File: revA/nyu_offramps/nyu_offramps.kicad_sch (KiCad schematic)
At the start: 88 parts, among them J15 Conn_02x06_Odd_Even, J16 Conn_01x24_Female, J17 Conn_01x24_Female, J19 Conn_01x06_Male, J23 Screw_Terminal_01x02, J24 Conn_01x03_Male, J25 Screw_Terminal_01x02, J3 Conn_01x04_Pin, J4 Conn_01x01, U1 MCP4725xxx-xCH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

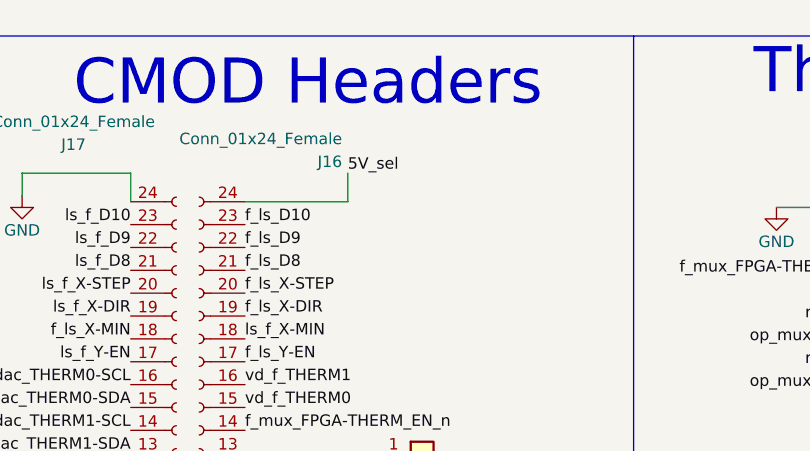
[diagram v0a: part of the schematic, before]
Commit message: Cleaned up and renamed project
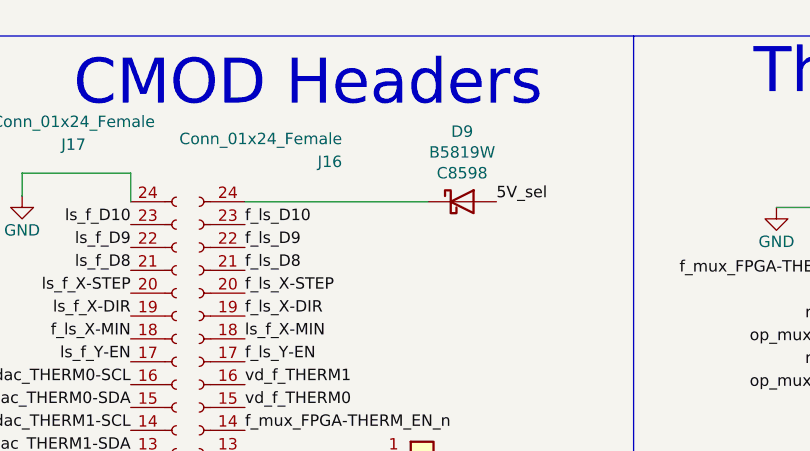
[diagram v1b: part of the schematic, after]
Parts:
- added D9: B5819W, Diode_SMD:D_SOD-123, symbol Device:D_Schottky
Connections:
- net 5V_sel: now also D9.2 (A); no longer J16.24 (Pin_24)
- new net: D9.1 (K), J16.24 (Pin_24)
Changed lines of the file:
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@@
     (stroke (width 0) (type solid))
   )
-  (wire (pts (xy 201.93 32.385) (xy 190.5 32.385))
+  (wire (pts (xy 210.82 32.385) (xy 190.5 32.385))
     (stroke (width 0) (type default))
   )
@@
     (stroke (width 0) (type solid))
   )
-  (wire (pts (xy 201.93 29.21) (xy 201.93 32.385))
-    (stroke (width 0) (type default))
-  )
   (wire (pts (xy 79.375 40.005) (xy 64.135 40.005))
     (stroke (width 0) (type solid))
@@
     (effects (font (size 1.27 1.27)) (justify right bottom))
   )
-  (label "5V_sel" (at 201.93 29.21 0) (fields_autoplaced)
+  (label "5V_sel" (at 218.44 32.385 0) (fields_autoplaced)
     (effects (font (size 1.27 1.27)) (justify left bottom))
   )
@@
         )
       )
+    )
+  )
+  (symbol (lib_id "Device:D_Schottky") (at 214.63 32.385 0) (unit 1)
+    (in_bom yes) (on_board yes) (dnp no)
+    (property "Reference" "D9" (at 214.63 24.5872 0)
+      (effects (font (size 1.27 1.27)))
+    )
+    (property "Value" "B5819W" (at 214.63 26.8986 0)
+      (effects (font (size 1.27 1.27)))
+    )
+    (property "Footprint" "Diode_SMD:D_SOD-123" (at 214.63 32.385 0)
+      (effects (font (size 1.27 1.27)) hide)
+    )
+    (property "Datasheet" "~" (at 214.63 32.385 0)
+      (effects (font (size 1.27 1.27)) hide)
+    )
+    (property "Vendor" "C8598" (at 214.63 29.21 0)
+      (effects (font (size 1.27 1.27)))
+    )
+    (pin "1")
+    (pin "2")
+    (instances
+      (project "nyu_pcb_link_te"
+        (path "/80f8c1b4-10dd-40fe-b7f7-67988bc3ad81"
+          (reference "D9") (unit 1)
+        )
+      )
+      (project "cmods7_trojan_shield"
+        (path "/e63e39d7-6ac0-4ffd-8aa3-1841a4541b55"
+          (reference "D2") (unit 1)
+        )
+      )
